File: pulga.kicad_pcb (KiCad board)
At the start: 2 copper layers, 38 x 34 mm, 30 parts, among them J1 Conn_01x02_Socket, J2 Conn_01x02_Socket, J3 Conn_01x02_Socket, J4 Conn_01x02_Socket, U2 ESP32-C3-WROOM-02, U3 TCAN332G, U4 AMS1117-3.3

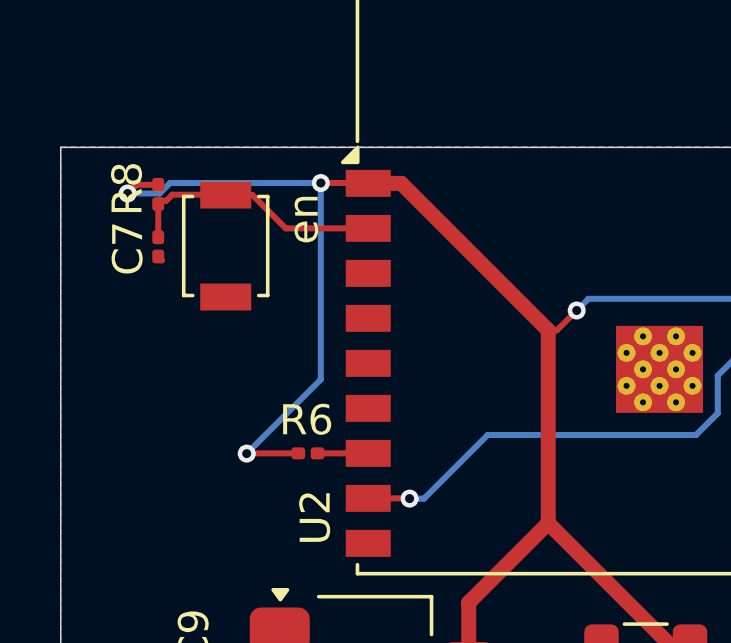
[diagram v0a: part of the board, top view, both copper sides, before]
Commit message: mudando a posição da via de R6
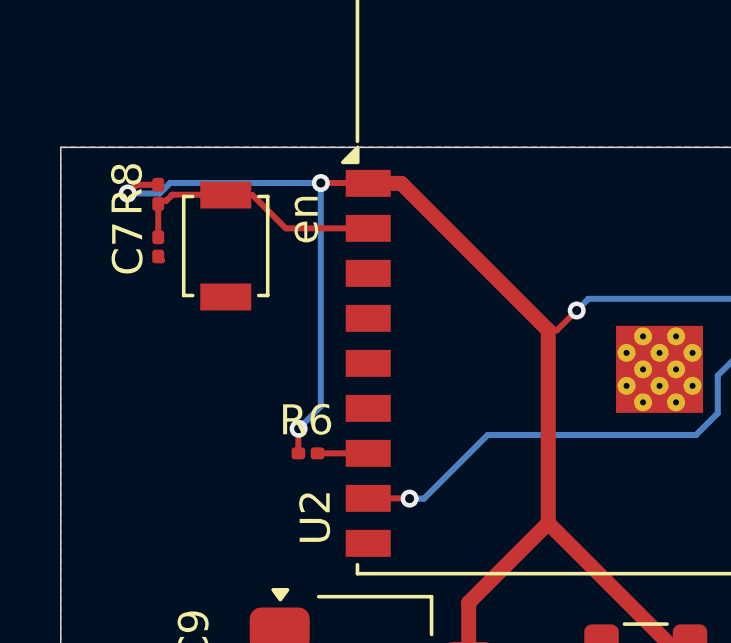
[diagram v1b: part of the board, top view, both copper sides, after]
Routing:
- net 3V3: track 101.9 -> 99.4 mm
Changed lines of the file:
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@@
-	)
-	(segment
-		(start 135.0075 93.7625)
-		(end 135 93.77)
-		(width 0.2)
-		(layer "F.Cu")
-		(net 10)
 	)
 	(segment
@@
 	)
 	(segment
-		(start 136.72 93.7625)
-		(end 135.0075 93.7625)
-		(width 0.2)
-		(layer "F.Cu")
-		(net 10)
-	)
-	(segment
 		(start 164.8 88.73)
 		(end 164.8 89.69)
@@
 	)
 	(segment
+		(start 136.72 92.95)
+		(end 136.73 92.94)
+		(width 0.2)
+		(layer "F.Cu")
+		(net 10)
+	)
+	(segment
 		(start 158.75 88.58)
 		(end 158.75 88.55)
@@
 	)
 	(segment
+		(start 136.72 93.7625)
+		(end 136.72 92.95)
+		(width 0.2)
+		(layer "F.Cu")
+		(net 10)
+	)
+	(segment
 		(start 163.699999 88.82)
 		(end 164.38 88.139999)
@@
 	)
 	(via
-		(at 135 93.77)
+		(at 136.73 92.94)
 		(size 0.6)
 		(drill 0.3)
@@
 	(segment
 		(start 137.47 84.75)
-		(end 137.47 91.3)
+		(end 137.47 92.2)
 		(width 0.2)
 		(layer "B.Cu")
@@
 	)
 	(segment
+		(start 137.47 92.2)
+		(end 136.73 92.94)
+		(width 0.2)
+		(layer "B.Cu")
+		(net 10)
+	)
+	(segment
 		(start 163.76 89.47)
 		(end 164.38 88.85)
 		(width 0.2)
 		(layer "B.Cu")
-		(net 10)
-	)
-	(segment
-		(start 137.47 91.3)
-		(end 135 93.77)
-		(width 0.2)
-		(layer "B.Cu")

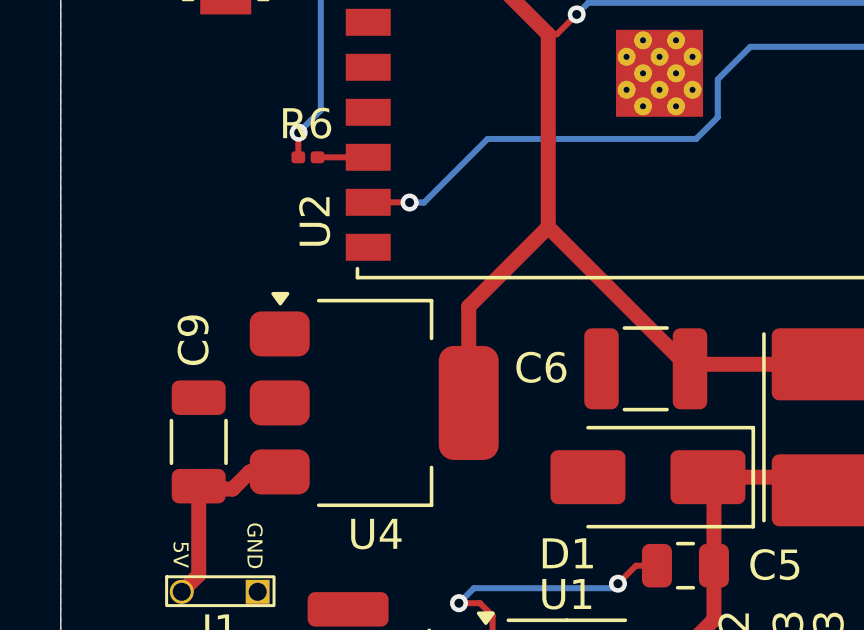
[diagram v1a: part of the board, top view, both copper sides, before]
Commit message: trocando o pino de 3V3 do AMS1117 para o 2 e não o "dissipador"
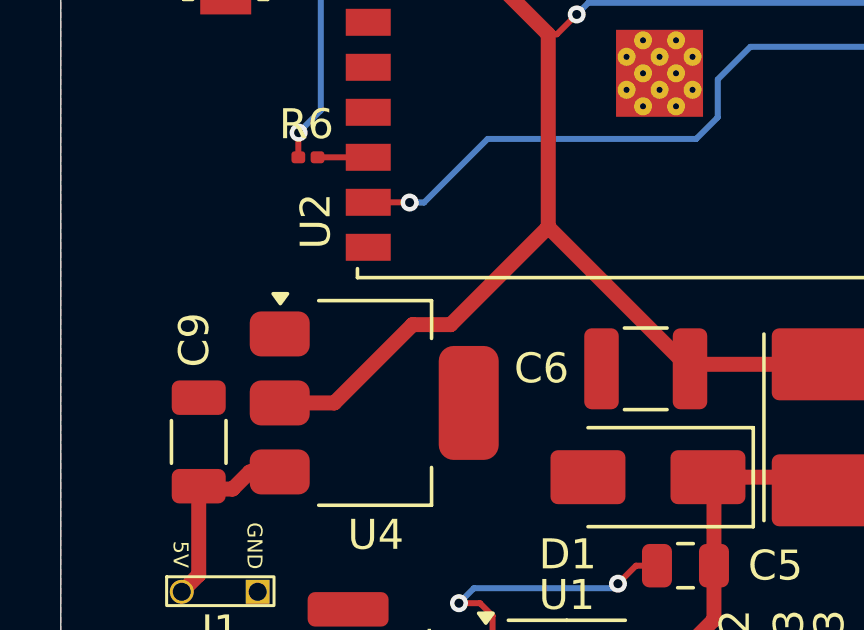
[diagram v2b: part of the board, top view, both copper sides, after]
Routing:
- net 3V3: track 99.4 -> 103.9 mm
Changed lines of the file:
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@@
-	)
-	(segment
-		(start 145.050875 96.0875)
-		(end 142.4 98.738375)
-		(width 0.5)
-		(layer "F.Cu")
-		(net 10)
-	)
-	(segment
-		(start 142.4 98.738375)
-		(end 142.4 101.95)
-		(width 0.5)
-		(layer "F.Cu")
-		(net 10)
 	)
 	(segment
@@
 		(end 158.75 88.58)
 		(width 0.2)
+		(layer "F.Cu")
+		(net 10)
+	)
+	(segment
+		(start 141.798375 99.34)
+		(end 140.53 99.34)
+		(width 0.5)
 		(layer "F.Cu")
 		(net 10)
@@
 	)
 	(segment
+		(start 145.050875 96.0875)
+		(end 141.798375 99.34)
+		(width 0.5)
+		(layer "F.Cu")
+		(net 10)
+	)
+	(segment
 		(start 137.47 84.75)
 		(end 138.978375 84.75)
@@
 	)
 	(segment
+		(start 140.53 99.34)
+		(end 137.92 101.95)
+		(width 0.5)
+		(layer "F.Cu")
+		(net 10)
+	)
+	(segment
 		(start 149.95 99.825)
 		(end 149.85 99.925)
 		(width 0.5)
 		(layer "F.Cu")
+		(net 10)
+	)
+	(segment
+		(start 137.92 101.95)
+		(end 136.1 101.95)
+		(width 0.5)
+		(layer "F.Cu")
